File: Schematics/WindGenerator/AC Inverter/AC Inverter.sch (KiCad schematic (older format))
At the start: 18 parts, among them Q1 BS170, Q2 BC337, Q3 BC327

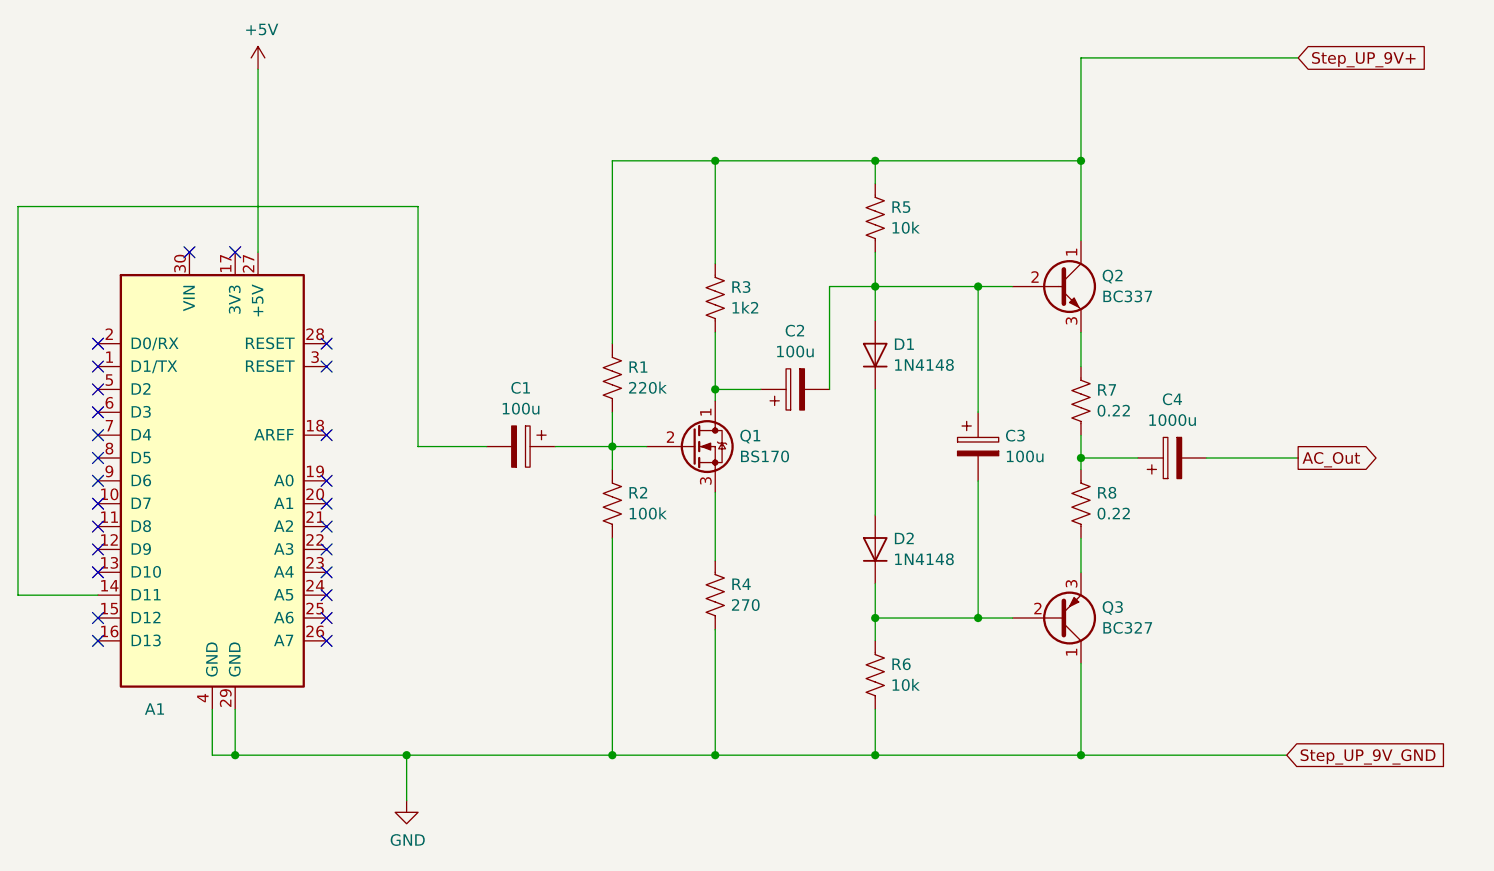
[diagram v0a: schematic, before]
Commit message: Modify AC Inverter schematic
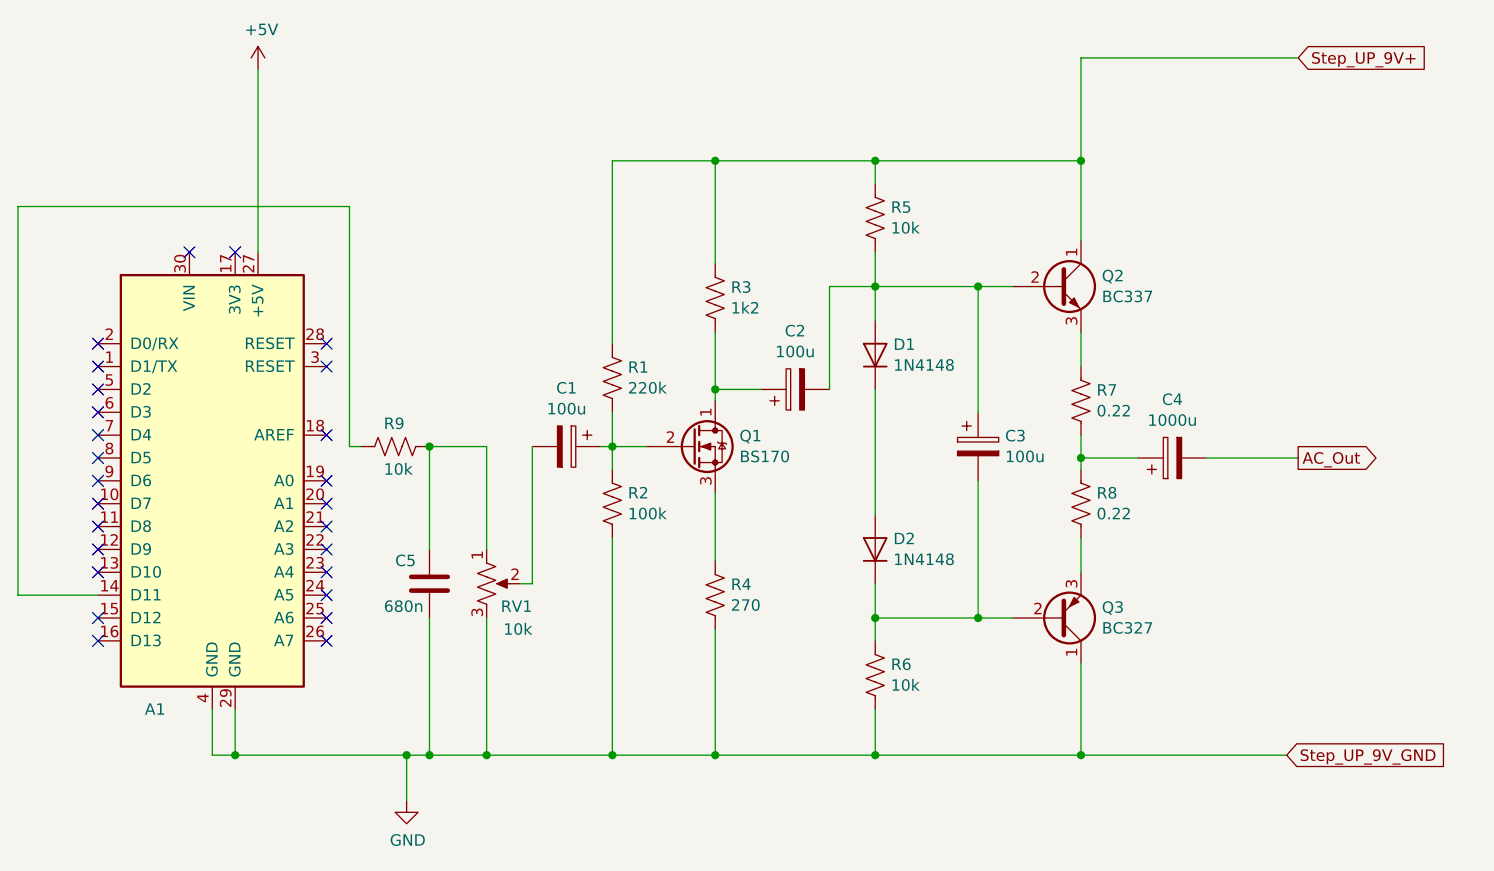
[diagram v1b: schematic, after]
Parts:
- added C5: 680n, symbol Device:C
- added R9: 10k, symbol Device:R_US
- added RV1: 10k, symbol Device:R_POT_US
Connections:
- net GND: now also C5.2, RV1.3
- net at A1.14 (D11): now also R9.2; no longer C1.2
- new net: C5.1, R9.1, RV1.1
- new net: C1.2, RV1.2
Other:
- moved on the sheet: C1
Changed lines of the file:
@@
 	5050 3650 5050 4600
 Wire Wire Line
-	5050 4600 4150 4600
+	5050 4600 4500 4600
 Wire Wire Line
 	3300 4600 3300 4400
@@
 L Device:CP C1
 U 1 1 5CA59F0A
-P 4650 3250
-F 0 "C1" V 4395 3250 50  0000 C CNN
-F 1 "100u" V 4486 3250 50  0000 C CNN
-F 2 "" H 4688 3100 50  0001 C CNN
-F 3 "~" H 4650 3250 50  0001 C CNN
-	1    4650 3250
+P 4850 3250
+F 0 "C1" V 4595 3250 50  0000 C CNN
+F 1 "100u" V 4686 3250 50  0000 C CNN
+F 2 "" H 4888 3100 50  0001 C CNN
+F 3 "~" H 4850 3250 50  0001 C CNN
+	1    4850 3250
 	0    1    1    0
 $EndComp
 Wire Wire Line
-	4800 3250 5050 3250
-Wire Wire Line
-	4500 3250 4200 3250
-Wire Wire Line
-	4200 3250 4200 2200
-Wire Wire Line
-	4200 2200 2450 2200
+	5000 3250 5050 3250
+Wire Wire Line
+	3900 2200 2450 2200
 Wire Wire Line
 	2450 2200 2450 3900
@@
 	1    0    0    -1
 $EndComp
+$Comp
+L Device:C C5
+U 1 1 5C937B4E
+P 4250 3850
+F 0 "C5" H 4100 3950 50  0000 L CNN
+F 1 "680n" H 4050 3750 50  0000 L CNN
+F 2 "" H 4288 3700 50  0001 C CNN
+F 3 "~" H 4250 3850 50  0001 C CNN
+	1    4250 3850
+	1    0    0    -1
+$EndComp
+Wire Wire Line
+	4250 4000 4250 4600
+Connection ~ 4250 4600
+Wire Wire Line
+	4250 4600 4150 4600
+$Comp
+L Device:R_US R9
+U 1 1 5C93918F
+P 4100 3250
+F 0 "R9" V 4000 3200 50  0000 L CNN
+F 1 "10k" V 4200 3200 50  0000 L CNN
+F 2 "" V 4140 3240 50  0001 C CNN
+F 3 "~" H 4100 3250 50  0001 C CNN
+	1    4100 3250
+	0    1    1    0
+$EndComp
+Wire Wire Line
+	4250 3700 4250 3250
+Wire Wire Line
+	3900 2200 3900 3250
+Wire Wire Line
+	3900 3250 3950 3250
+$Comp
+L Device:R_POT_US RV1
+U 1 1 5C93F1B7
+P 4500 3850
+F 0 "RV1" H 4700 3750 50  0000 R CNN
+F 1 "10k" H 4700 3650 50  0000 R CNN
+F 2 "" H 4500 3850 50  0001 C CNN
+F 3 "~" H 4500 3850 50  0001 C CNN
+	1    4500 3850
+	1    0    0    -1
+$EndComp
+Wire Wire Line
+	4500 4000 4500 4600
+Connection ~ 4500 4600
+Wire Wire Line
+	4500 4600 4250 4600
+Wire Wire Line
+	4500 3700 4500 3250
+Wire Wire Line
+	4500 3250 4250 3250
+Connection ~ 4250 3250
+Wire Wire Line
+	4700 3250 4700 3850
+Wire Wire Line
+	4700 3850 4650 3850
 $EndSCHEMATC

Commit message: Modify AC invert to use LM386
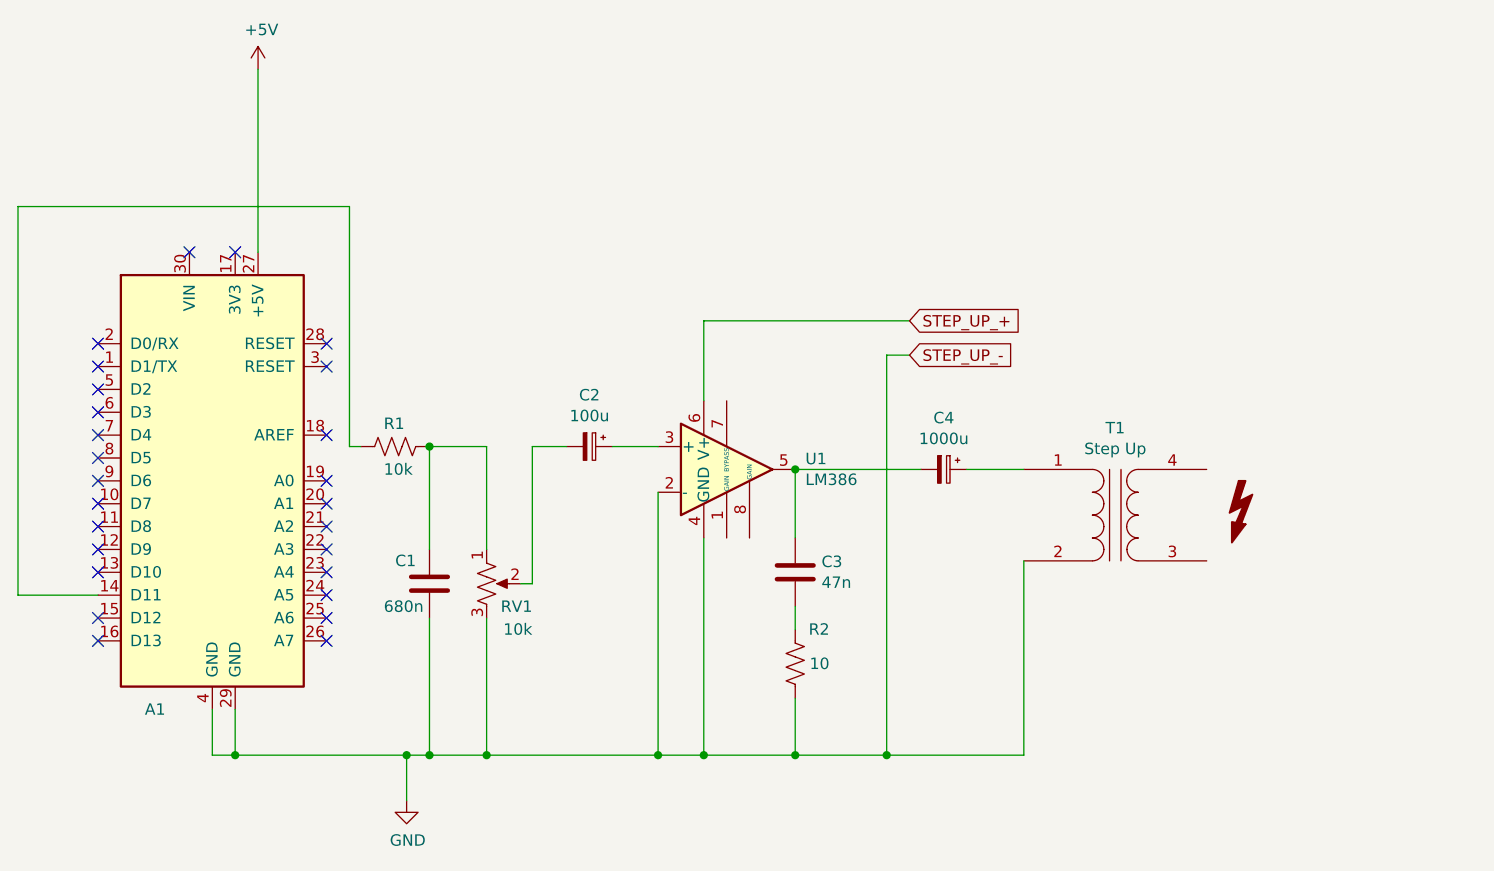
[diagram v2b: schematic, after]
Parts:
- removed C1, C2, C3: 100u, symbol Device:CP
- removed C4: 1000u, symbol Device:CP
- removed D1, D2: 1N4148, Diode_THT:D_DO-35_SOD27_P7.62mm_Horizontal, symbol Diode:1N4148
- removed Q1: BS170, Package_TO_SOT_THT:TO-92_Inline, symbol Transistor_FET:BS170
- removed Q2: BC337, Package_TO_SOT_THT:TO-92_Inline, symbol Transistor_BJT:BC337
- removed Q3: BC327, Package_TO_SOT_THT:TO-92_Inline, symbol Transistor_BJT:BC327
- removed R1: 220k, symbol Device:R_US
- removed R3: 1k2, symbol Device:R_US
- removed R4: 270, symbol Device:R_US
- removed R5, R6: 10k, symbol Device:R_US
- removed R7, R8: 0.22, symbol Device:R_US
- added C2: 100u, symbol Device:CP_Small
- added C3: 47n, symbol Device:C
- added C4: 1000u, symbol Device:CP_Small
- added T1: Step Up, symbol Device:Transformer_1P_1S
- added U1: LM386, symbol Amplifier_Audio:LM386
- R2: value 100k -> 10
- renumbered C5 to C1, R9 to R1
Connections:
- net GND: now also R2.1, T1.2 (AB), U1.2 (-), U1.4 (GND); no longer R2.2
- net at RV1.2: now also C2.2
- new net: C2.1, U1.3 (+)
- new net: C3.1, C4.2, U1.5
- new net: C3.2, R2.2
- new net: C4.1, T1.1 (AA)
- new net STEP_UP_+: U1.6 (V+)
